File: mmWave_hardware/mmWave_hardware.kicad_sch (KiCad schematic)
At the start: 51 parts, among them J1 Conn_02x08_Top_Bottom, U1 IWRL6432BDBAAMFR, U2 W25Q128JVS, U3 AMS1117-3.3, U4 TPS628502QDRLRQ1, Y1 40.000

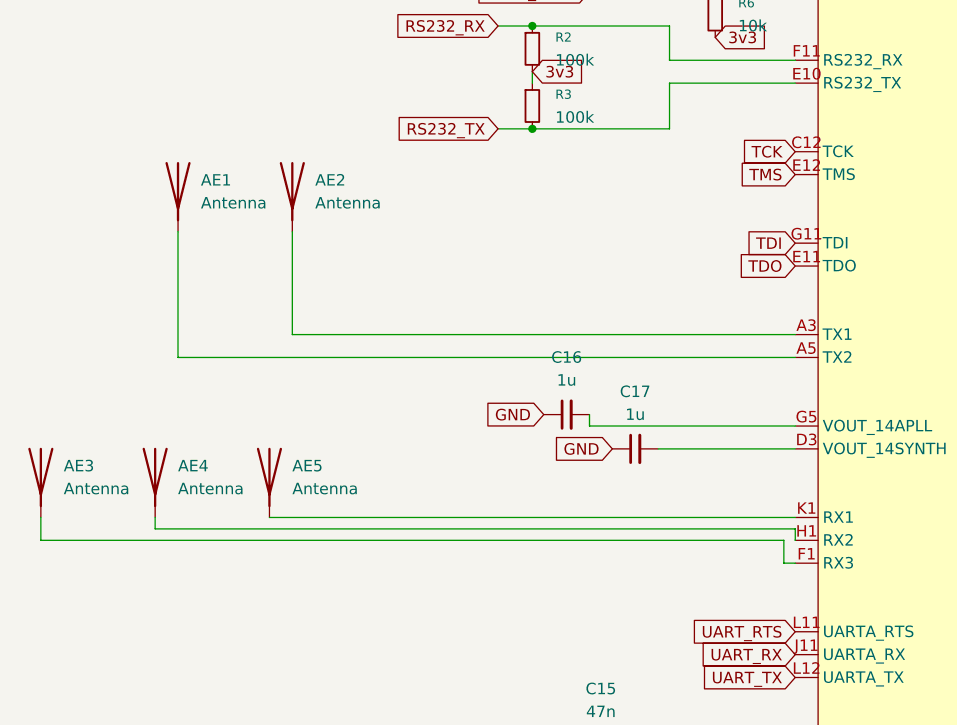
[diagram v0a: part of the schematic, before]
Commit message: antennas(RX+TX)
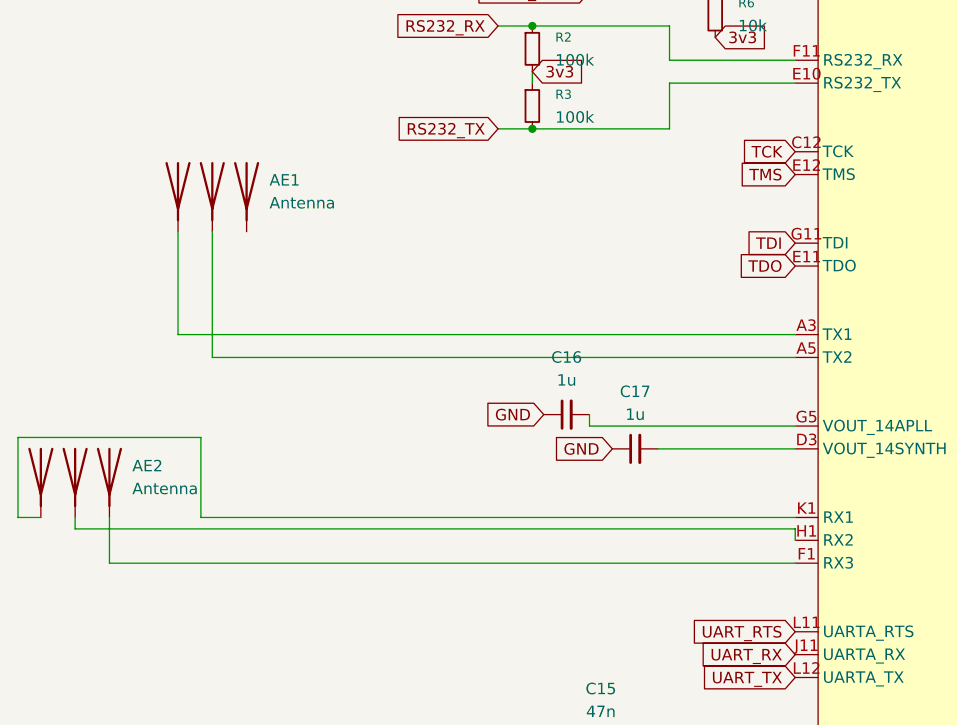
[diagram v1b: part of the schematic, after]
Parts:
- removed AE1, AE2, AE3, AE4, AE5: Antenna, antennas:60GHz_microstrip_inset_patch, symbol Device:Antenna
- added AE1: Antenna, antennas:TX_60GHz_microstrip_inset_patch, symbol Device:Antenna_1
- added AE2: Antenna, antennas:RX_60GHz_microstrip_inset_patch, symbol Device:Antenna_1
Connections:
- net at U1.A3 (TX1): now also AE1.1 (A)
- net at U1.K1 (RX1): now also AE2.1 (A)
- net at U1.A5 (TX2): now also AE1.2 (A)
- net at U1.H1 (RX2): now also AE2.2 (A)
- net at U1.F1 (RX3): now also AE2.3 (A)

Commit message: PCB Complete
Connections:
- net GPIO_2: now also J1.2 (Pin_2)
- net GPIO_5: now also J1.4 (Pin_4)
- net TCK: no longer J1.2 (Pin_2)
- net TDI: no longer J1.4 (Pin_4)
- net TDO: no longer J1.5 (Pin_5)
- net TMS: no longer J1.3 (Pin_3)

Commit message: pcb
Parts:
- Y1: footprint Crystal:Crystal_SMD_3225-4Pin_3.2x2.5mm_HandSoldering -> Crystal:Crystal_SMD_3225-4Pin_3.2x2.5mm
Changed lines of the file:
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@@
 			)
 		)
-		(property "Footprint" "Crystal:Crystal_SMD_3225-4Pin_3.2x2.5mm_HandSoldering"
+		(property "Footprint" "Crystal:Crystal_SMD_3225-4Pin_3.2x2.5mm"
 			(at 87.63 67.31 0)
 			(effects

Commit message: PCB Done
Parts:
- TP1, TP2, TP3, TP4, TP5: footprint TestPoint:TestPoint_Pad_D1.5mm -> TestPoint:TestPoint_Pad_D1.0mm
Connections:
- net GND: now also J1.3 (Pin_3), J1.5 (Pin_5)
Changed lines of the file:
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@@
 		)
 	)
+	(global_label "GND"
+		(shape input)
+		(at 72.39 218.44 180)
+		(fields_autoplaced yes)
+		(effects
+			(font
+				(size 1.27 1.27)
+			)
+			(justify right)
+		)
+		(property "Intersheetrefs" "${INTERSHEET_REFS}"
+			(at 65.5343 218.44 0)
+			(effects
+				(font
+					(size 1.27 1.27)
+				)
+				(justify right)
+				(hide yes)
+			)
+		)
+	)
 	(global_label "VDD_SRAM"
 		(shape input)
@@
 		)
 	)
+	(global_label "GND"
+		(shape input)
+		(at 72.39 213.36 180)
+		(fields_autoplaced yes)
+		(effects
+			(font
+				(size 1.27 1.27)
+			)
+			(justify right)
+		)
+		(property "Intersheetrefs" "${INTERSHEET_REFS}"
+			(at 65.5343 213.36 0)
+			(effects
+				(font
+					(size 1.27 1.27)
+				)
+				(justify right)
+				(hide yes)
+			)
+		)
+	)
 	(global_label "UART_RX"
 		(shape input)
@@
 			)
 		)
-		(property "Footprint" "TestPoint:TestPoint_Pad_D1.5mm"
+		(property "Footprint" "TestPoint:TestPoint_Pad_D1.0mm"
 			(at 300.99 106.68 0)
 			(effects
@@
 			)
 		)
-		(property "Footprint" "TestPoint:TestPoint_Pad_D1.5mm"
+		(property "Footprint" "TestPoint:TestPoint_Pad_D1.0mm"
 			(at 300.99 111.76 0)
 			(effects
@@
 			)
 		)
-		(property "Footprint" "TestPoint:TestPoint_Pad_D1.5mm"
+		(property "Footprint" "TestPoint:TestPoint_Pad_D1.0mm"
 			(at 275.59 97.79 0)
 			(effects
@@
 			)
 		)
-		(property "Footprint" "TestPoint:TestPoint_Pad_D1.5mm"
+		(property "Footprint" "TestPoint:TestPoint_Pad_D1.0mm"
 			(at 127 87.63 0)
 			(effects
@@
 			)
 		)
-		(property "Footprint" "TestPoint:TestPoint_Pad_D1.5mm"
+		(property "Footprint" "TestPoint:TestPoint_Pad_D1.0mm"
 			(at 275.59 102.87 0)
 			(effects

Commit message: PCB
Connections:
- net TCK: no longer names the net of U1.C12 (TCK)
- net TDI: no longer names the net of U1.G11 (TDI)
- net TDO: no longer names the net of U1.E11 (TDO)
- net TMS: no longer names the net of U1.E12 (TMS)
- no-connect marks 2 -> 6

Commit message: routing done
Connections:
- net GND: no longer J1.3 (Pin_3), J1.5 (Pin_5)
- net GPIO_2: now also J1.3 (Pin_3); no longer J1.2 (Pin_2)
- net NRST_MAIN: now also J1.8 (Pin_8); no longer J1.15 (Pin_15)
- net RS232_RX: now also J1.5 (Pin_5); no longer J1.14 (Pin_14)
- net RS232_TX: now also J1.6 (Pin_6); no longer J1.13 (Pin_13)
- net SPI0_CLK: now also J1.14 (Pin_14); no longer J1.9 (Pin_9)
- net SPI0_CS0_N: now also J1.13 (Pin_13); no longer J1.10 (Pin_10)
- net SPI0_MISO: now also J1.16 (Pin_16); no longer J1.11 (Pin_11)
- net SPI0_MOSI: now also J1.15 (Pin_15); no longer J1.12 (Pin_12)
- net UART_RTS: now also J1.10 (Pin_10); no longer J1.6 (Pin_6)
- net UART_RX: now also J1.11 (Pin_11); no longer J1.7 (Pin_7)
- net UART_TX: now also J1.12 (Pin_12); no longer J1.8 (Pin_8)
- net VIN: now also J1.2 (Pin_2); no longer J1.16 (Pin_16)

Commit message: fixed footprint issue
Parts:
- C18, C19, C20, C21: footprint Capacitor_SMD:C_0603_1608Metric -> Capacitor_SMD:C_0603_1608Metric_Pad1.08x0.95mm_HandSolder
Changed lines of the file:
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@@
 			)
 		)
-		(property "Footprint" "Capacitor_SMD:C_0603_1608Metric"
+		(property "Footprint" "Capacitor_SMD:C_0603_1608Metric_Pad1.08x0.95mm_HandSolder"
 			(at 313.69 66.04 0)
 			(effects
@@
 			)
 		)
-		(property "Footprint" "Capacitor_SMD:C_0603_1608Metric"
+		(property "Footprint" "Capacitor_SMD:C_0603_1608Metric_Pad1.08x0.95mm_HandSolder"
 			(at 275.59 31.75 0)
 			(effects
@@
 			)
 		)
-		(property "Footprint" "Capacitor_SMD:C_0603_1608Metric"
+		(property "Footprint" "Capacitor_SMD:C_0603_1608Metric_Pad1.08x0.95mm_HandSolder"
 			(at 309.88 66.04 0)
 			(effects
@@
 			)
 		)
-		(property "Footprint" "Capacitor_SMD:C_0603_1608Metric"
+		(property "Footprint" "Capacitor_SMD:C_0603_1608Metric_Pad1.08x0.95mm_HandSolder"
 			(at 294.64 31.75 0)
 			(effects

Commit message: changed silkscreen
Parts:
- R8: footprint Resistor_SMD:R_0402_1005Metric -> Resistor_SMD:R_0402_1005Metric_Pad0.72x0.64mm_HandSolder
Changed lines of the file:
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@@
 			)
 		)
-		(property "Footprint" "Resistor_SMD:R_0402_1005Metric"
+		(property "Footprint" "Resistor_SMD:R_0402_1005Metric_Pad0.72x0.64mm_HandSolder"
 			(at 321.31 72.39 0)
 			(effects
